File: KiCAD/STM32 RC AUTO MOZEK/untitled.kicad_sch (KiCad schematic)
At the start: 18 parts, among them J9 Conn_01x03_Socket, Q1 SI2312, Q10 SI2312, Q11 SI2312, Q12 SI2312, Q2 SI2312, Q3 SI2312, Q4 SI2312, Q5 SI2312, Q6 SI2312, Q7 SI2312, Q8 SI2312, Q9 SI2312, U12 STM32F411RCTx, U6 NRF24L01_Breakout

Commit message: i dont know
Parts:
- removed J9: Conn_01x03_Socket, Connector_Wire:SolderWire-0.5sqmm_1x03_P4.6mm_D0.9mm_OD2.1mm_Relief, symbol Connector:Conn_01x03_Socket
- added J10: Conn_01x05_Socket, Connector_Wire:SolderWire-0.5sqmm_1x05_P4.8mm_D0.9mm_OD2.3mm_Relief, symbol Connector:Conn_01x05_Socket
- added JP7: SolderJumper_3_Open, Jumper:SolderJumper-3_P1.3mm_Open_RoundedPad1.0x1.5mm_NumberLabels, symbol Jumper:SolderJumper_3_Open
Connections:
- net GND: now also J10.1 (Pin_1)
- net at Q5.1, Q6.1: now also U12.11 (PC3)
- net at Q3.1, Q4.1: now also U12.10 (PC2)
- net at Q10.1, Q9.1: now also U12.8 (PC0)
- net at Q7.1, Q8.1: now also U12.24 (PC4)
- net at Q1.1, Q2.1: now also U12.9 (PC1)
- net at JP5.1 (A): now also J10.4 (Pin_4)
- net at Q11.1, Q12.1: now also U12.25 (PC5)
- net at JP4.1 (A): now also J10.3 (Pin_3)
- net at U12.20 (PA4): now also JP7.2 (C); no longer U6.4 (~{CSN})
- net at JP6.1 (A): now also J10.5 (Pin_5)
- new net: J10.2 (Pin_2), JP7.1 (A)
- new net: JP7.3 (B), U6.4 (~{CSN})

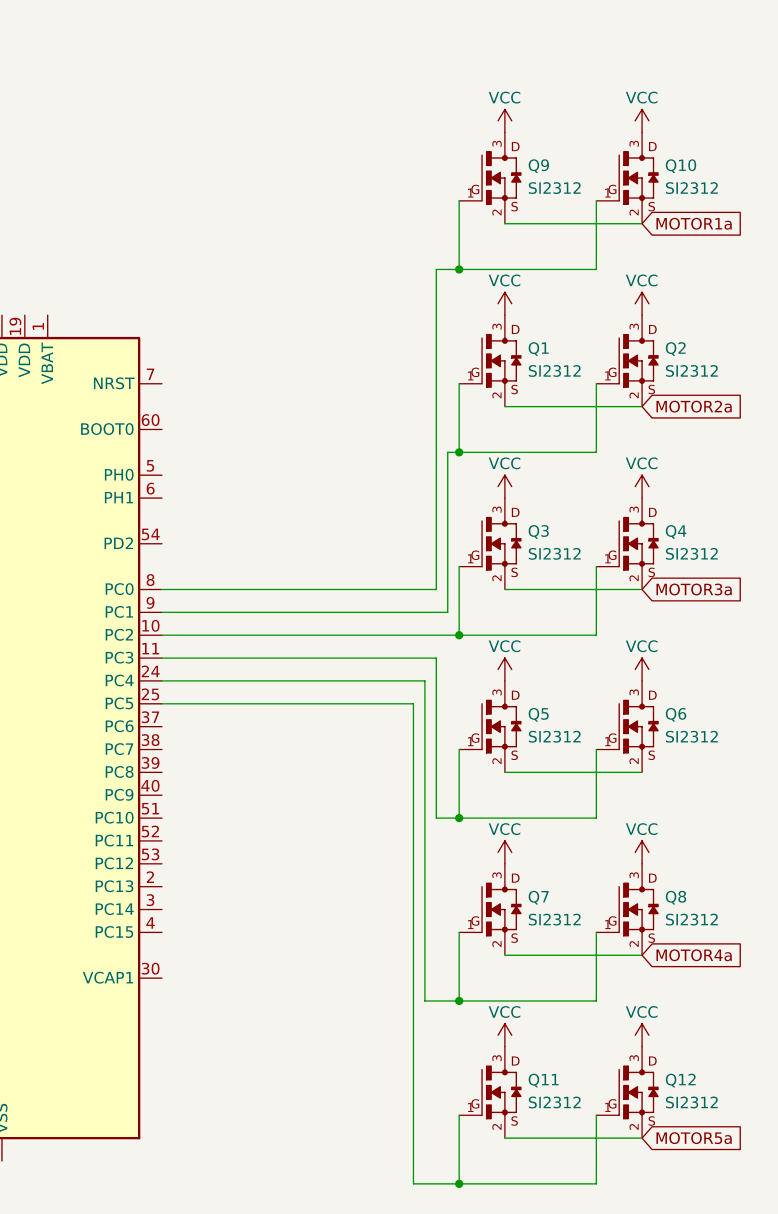
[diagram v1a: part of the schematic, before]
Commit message: Motor power brick implementation
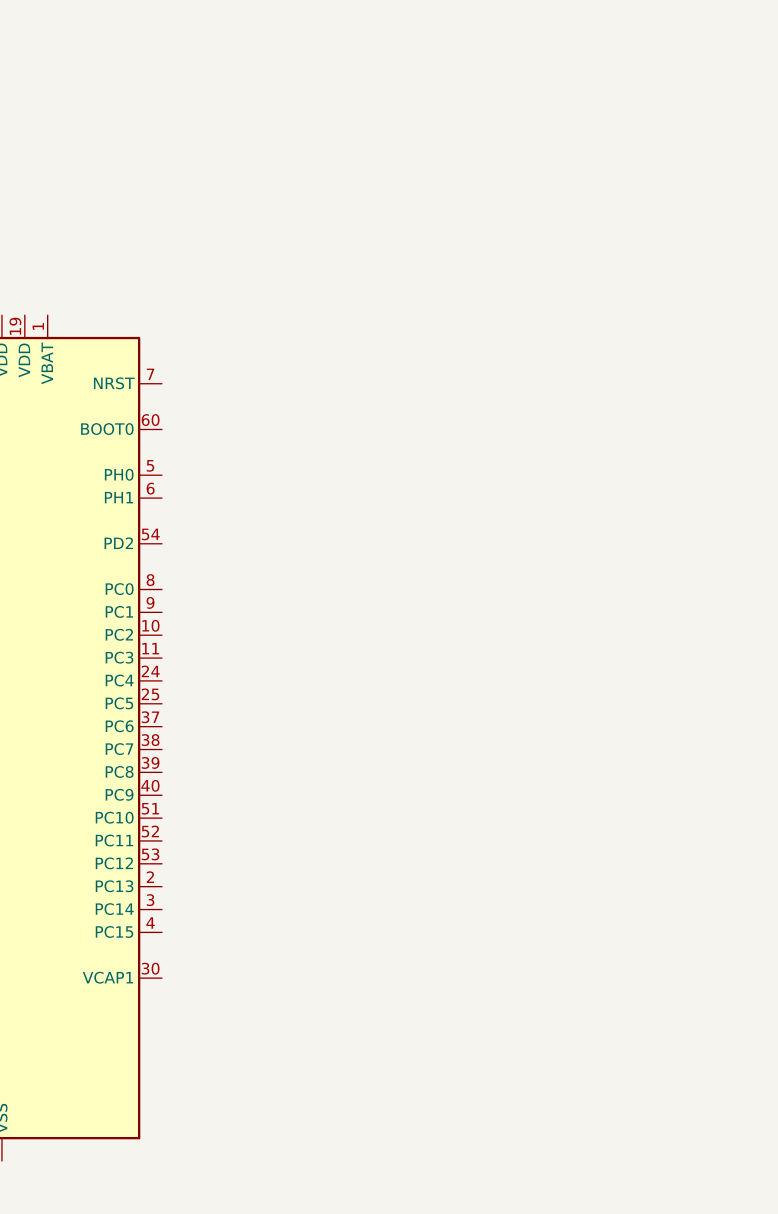
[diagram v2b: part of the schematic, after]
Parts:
- removed Q1, Q10, Q11, Q12, Q2, Q3, Q4, Q5, Q6, Q7, Q8, Q9: SI2312, SI2312:SOT23, symbol SI2312:SI2312

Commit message: Multi ADD
Completed work version of code and did more work on schematic
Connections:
- net MOTOR2a: now reaches U12.10 (PC2)
- net MOTOR2b: now reaches U12.11 (PC3)
- net MOTOR3a: now reaches U12.24 (PC4)
- net MOTOR3b: now reaches U12.25 (PC5)
- net PWM1: now reaches U12.26 (PB0)
- net PWM2: now reaches U12.27 (PB1)
- net MOTOR4a: now reaches U12.37 (PC6)
- net MOTOR4b: now reaches U12.38 (PC7)
- net MOTOR5a: now reaches U12.39 (PC8)
- net MOTOR5b: now reaches U12.40 (PC9)
- net MOTOR6a: now reaches U12.51 (PC10)
- net MOTOR6b: now reaches U12.52 (PC11)
- net MOTOR1a: now reaches U12.8 (PC0)
- net MOTOR1b: now reaches U12.9 (PC1)

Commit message: .
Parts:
- added C11, C12, C13, C14: 12,5pF, Capacitor_SMD:C_0805_2012Metric_Pad1.18x1.45mm_HandSolder, symbol Device:C
- added J3, J4: Conn_01x03_Socket, Connector_JST:JST_XH_B3B-XH-A_1x03_P2.50mm_Vertical, symbol Connector:Conn_01x03_Socket
- added J5, J6: Conn_01x02_Socket, Connector_JST:JST_XH_B2B-XH-A_1x02_P2.50mm_Vertical, symbol Connector:Conn_01x02_Socket
- added Q49, Q50, Q51, Q52: SI2312, SI2312:SOT23, symbol SI2312:SI2312
- added Y3: 25MHz, Crystal:Crystal_SMD_HC49-SD, symbol Device:Crystal
- added Y4: 32.786KHz, Crystal:Crystal_DS26_D2.0mm_L6.0mm_Horizontal, symbol Device:Crystal
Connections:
- net GND: now also C11.2, C12.1, C13.2, C14.1, J3.3 (Pin_3), J4.3 (Pin_3), J5.2 (Pin_2), J6.2 (Pin_2)
- net PWM1: now also Q51.1
- net PWM2: now also Q52.1
- net PWM3: now reaches U12.28 (PB2)
- net PWM3: now also Q49.1
- net at U12.3 (PC14): now also C14.2, Y4.1
- net at U12.4 (PC15): now also C13.1, Y4.2
- net at U12.5 (PH0): now also C12.2, Y3.1
- net PWM4: now reaches U12.55 (PB3)
- net PWM4: now also Q50.1
- net at U12.6 (PH1): now also C11.1, Y3.2
- new net: J5.1 (Pin_1), Q49.2
- new net: J3.2 (Pin_2), Q51.2
- new net: J6.1 (Pin_1), Q50.2
- new net: J4.2 (Pin_2), Q52.2
- new net +5V: J3.1 (Pin_1), J4.1 (Pin_1), Q49.3, Q50.3, Q51.3, Q52.3

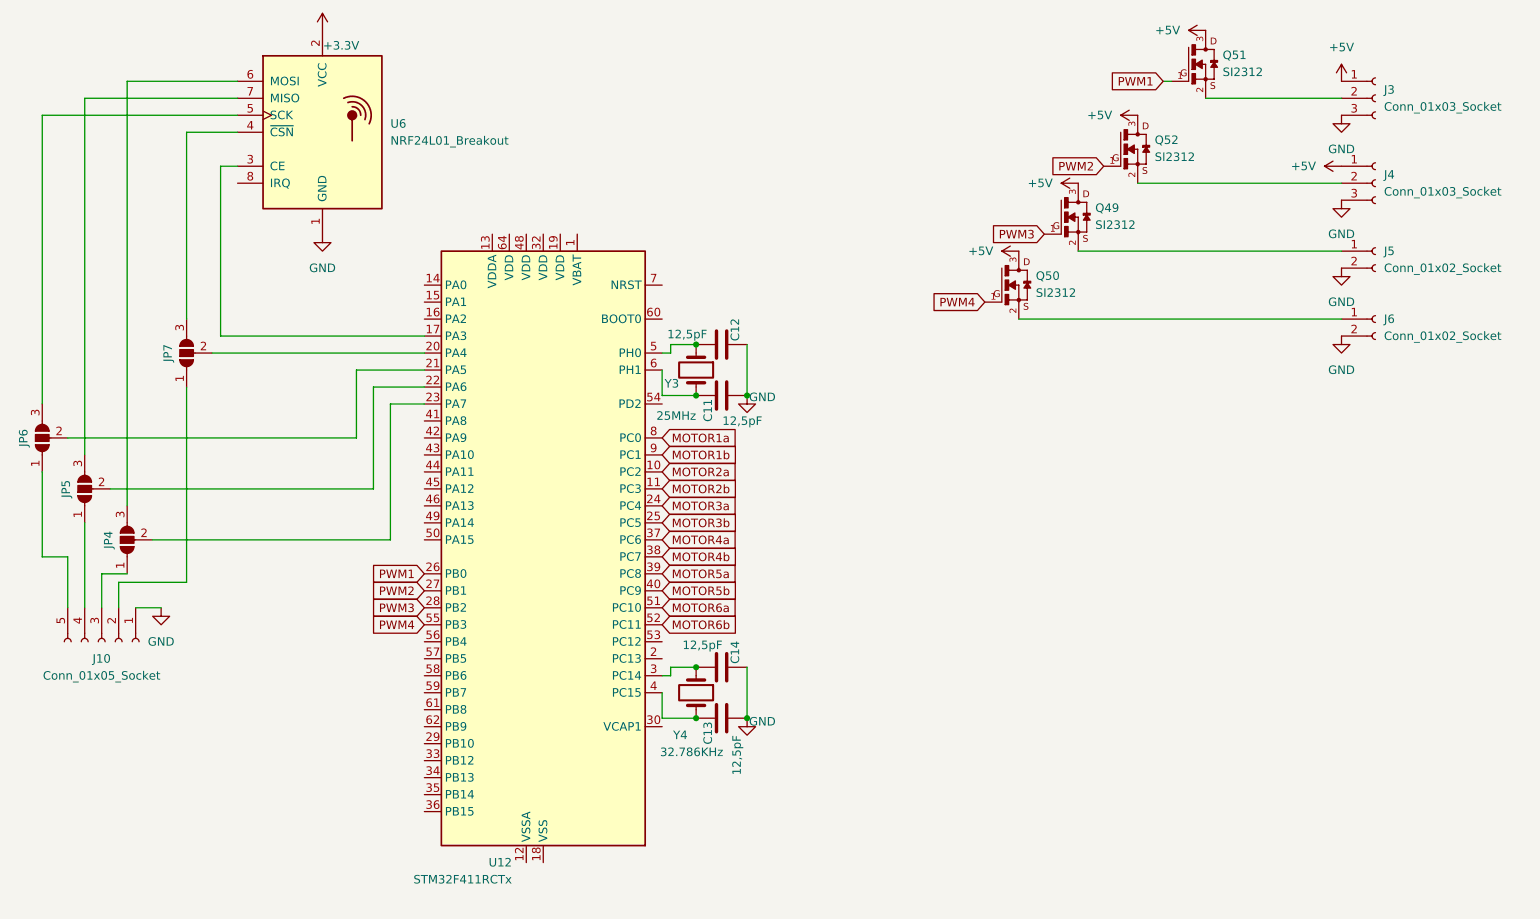
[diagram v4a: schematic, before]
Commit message: adding completation on schematic, working on board
need to add SWD Debug as input for programing
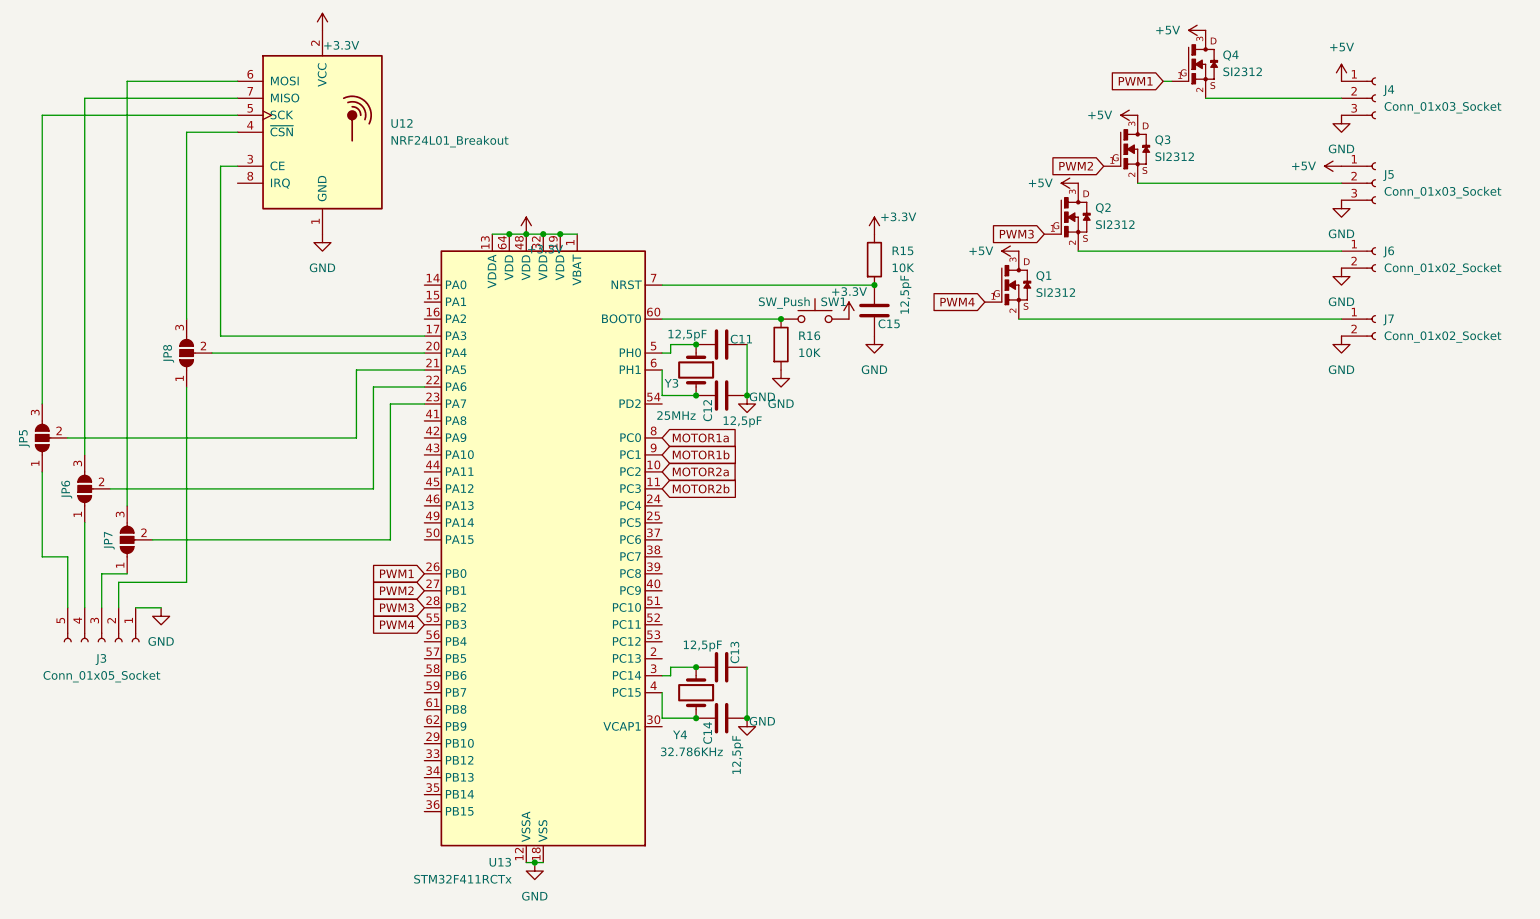
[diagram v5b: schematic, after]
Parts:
- added C15: 12,5pF, Capacitor_SMD:C_0805_2012Metric_Pad1.18x1.45mm_HandSolder, symbol Device:C
- added R15, R16: 10K, Resistor_SMD:R_0805_2012Metric_Pad1.20x1.40mm_HandSolder, symbol Device:R
- added SW1: SW_Push, Button_Switch_SMD:SW_SPST_CK_RS282G05A3, symbol Switch:SW_Push
- renumbered C12 to C11, C11 to C12, C14 to C13, C13 to C14, J10 to J3, J3 to J4, J4 to J5, J5 to J6, J6 to J7, JP6 to JP5, JP5 to JP6, JP4 to JP7, JP7 to JP8, Q50 to Q1, Q49 to Q2, Q52 to Q3, Q51 to Q4, U6 to U12, U12 to U13
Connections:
- net +3.3V: now also U13.1 (VBAT), U13.13 (VDDA), U13.19 (VDD), U13.32 (VDD), U13.48 (VDD), U13.64 (VDD), R15.1, SW1.2
- net GND: now also U13.12 (VSSA), U13.18 (VSS), U13.31 (VSS), U13.47 (VSS), U13.63 (VSS), C15.1, R16.2
- net at U13.60 (BOOT0): now also R16.1, SW1.1
- net at U13.7 (NRST): now also C15.2, R15.2
- net MOTOR3a: no longer names the net of U13.24 (PC4)
- net MOTOR3b: no longer names the net of U13.25 (PC5)
- net MOTOR4a: no longer names the net of U13.37 (PC6)
- net MOTOR4b: no longer names the net of U13.38 (PC7)
- net MOTOR5a: no longer names the net of U13.39 (PC8)
- net MOTOR5b: no longer names the net of U13.40 (PC9)
- net MOTOR6a: no longer names the net of U13.51 (PC10)
- net MOTOR6b: no longer names the net of U13.52 (PC11)

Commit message: .
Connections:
- net MOTOR1a: now also U13.37 (PC6); no longer U13.8 (PC0)
- net MOTOR1b: now also U13.38 (PC7); no longer U13.9 (PC1)
- net MOTOR2a: now also U13.39 (PC8); no longer U13.10 (PC2)
- net MOTOR2b: now also U13.40 (PC9); no longer U13.11 (PC3)
- net PWM1: now also U13.41 (PA8); no longer U13.26 (PB0)
- net PWM2: now also U13.42 (PA9); no longer U13.27 (PB1)
- net PWM3: now also U13.43 (PA10); no longer U13.28 (PB2)
- net PWM4: now also U13.44 (PA11); no longer U13.55 (PB3)
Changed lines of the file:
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@@
 	(wire
 		(pts
-			(xy 78.74 68.58) (xy 86.36 68.58)
+			(xy 54.61 68.58) (xy 86.36 68.58)
 		)
 		(stroke
@@
 	(wire
 		(pts
-			(xy 39.37 83.82) (xy 78.74 83.82)
+			(xy 39.37 83.82) (xy 54.61 83.82)
 		)
 		(stroke
@@
 	(wire
 		(pts
-			(xy 76.2 66.04) (xy 86.36 66.04)
+			(xy 53.34 66.04) (xy 86.36 66.04)
 		)
 		(stroke
@@
 	(wire
 		(pts
-			(xy 45.72 91.44) (xy 81.28 91.44)
-		)
-		(stroke
-			(width 0)
-			(type default)
-		)
-	)
-	(wire
-		(pts
-			(xy 78.74 83.82) (xy 78.74 68.58)
+			(xy 45.72 91.44) (xy 55.88 91.44)
+		)
+		(stroke
+			(width 0)
+			(type default)
+		)
+	)
+	(wire
+		(pts
+			(xy 54.61 83.82) (xy 54.61 68.58)
 		)
 		(stroke
@@
 	(wire
 		(pts
-			(xy 33.02 76.2) (xy 76.2 76.2)
+			(xy 33.02 76.2) (xy 53.34 76.2)
 		)
 		(stroke
@@
 	(wire
 		(pts
-			(xy 76.2 76.2) (xy 76.2 66.04)
+			(xy 53.34 76.2) (xy 53.34 66.04)
 		)
 		(stroke
@@
 	(wire
 		(pts
-			(xy 81.28 71.12) (xy 86.36 71.12)
+			(xy 55.88 71.12) (xy 86.36 71.12)
 		)
 		(stroke
@@
 	(wire
 		(pts
-			(xy 81.28 91.44) (xy 81.28 71.12)
+			(xy 55.88 91.44) (xy 55.88 71.12)
 		)
 		(stroke
@@
 	(global_label "PWM3"
 		(shape input)
-		(at 86.36 101.6 180)
+		(at 86.36 78.74 180)
 		(fields_autoplaced yes)
 		(effects
@@
 		)
 		(property "Intersheetrefs" "${INTERSHEET_REFS}"
-			(at 77.9925 101.6 0)
+			(at 77.9925 78.74 0)
 			(effects
 				(font
@@
 	(global_label "MOTOR2b"
 		(shape input)
-		(at 121.92 83.82 0)
+		(at 121.92 99.06 0)
 		(fields_autoplaced yes)
 		(effects
@@
 		)
 		(property "Intersheetrefs" "${INTERSHEET_REFS}"
-			(at 133.6137 83.82 0)
+			(at 133.6137 99.06 0)
 			(effects
 				(font
@@
 	(global_label "MOTOR1b"
 		(shape input)
-		(at 121.92 78.74 0)
+		(at 121.92 93.98 0)
 		(fields_autoplaced yes)
 		(effects
@@
 		)
 		(property "Intersheetrefs" "${INTERSHEET_REFS}"
-			(at 133.6137 78.74 0)
+			(at 133.6137 93.98 0)
 			(effects
 				(font
@@
 	(global_label "PWM2"
 		(shape input)
-		(at 86.36 99.06 180)
+		(at 86.36 76.2 180)
 		(fields_autoplaced yes)
 		(effects
@@
 		)
 		(property "Intersheetrefs" "${INTERSHEET_REFS}"
-			(at 77.9925 99.06 0)
+			(at 77.9925 76.2 0)
 			(effects
 				(font
@@
 	(global_label "MOTOR1a"
 		(shape input)
-		(at 121.92 76.2 0)
+		(at 121.92 91.44 0)
 		(fields_autoplaced yes)
 		(effects
@@
 		)
 		(property "Intersheetrefs" "${INTERSHEET_REFS}"
-			(at 133.6137 76.2 0)
+			(at 133.6137 91.44 0)
 			(effects
 				(font
@@
 	(global_label "MOTOR2a"
 		(shape input)
-		(at 121.92 81.28 0)
+		(at 121.92 96.52 0)
 		(fields_autoplaced yes)
 		(effects
@@
 		)
 		(property "Intersheetrefs" "${INTERSHEET_REFS}"
-			(at 133.6137 81.28 0)
+			(at 133.6137 96.52 0)
 			(effects
 				(font
@@
 	(global_label "PWM4"
 		(shape input)
-		(at 86.36 104.14 180)
+		(at 86.36 81.28 180)
 		(fields_autoplaced yes)
 		(effects
@@
 		)
 		(property "Intersheetrefs" "${INTERSHEET_REFS}"
-			(at 77.9925 104.14 0)
+			(at 77.9925 81.28 0)
 			(effects
 				(font
@@
 	(global_label "PWM1"
 		(shape input)
-		(at 86.36 96.52 180)
+		(at 86.36 73.66 180)
 		(fields_autoplaced yes)
 		(effects
@@
 		)
 		(property "Intersheetrefs" "${INTERSHEET_REFS}"
-			(at 77.9925 96.52 0)
-			(effects
-				(font
+			(at 77.9925 73.66 0)
+			(effects
+				(font
